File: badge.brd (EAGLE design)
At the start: 85 x 55 mm, 60 parts, among them J1 SJ-3523-SMT-TR, Q1 MMBT2222A-7-FSOT-23_DIO-M, Q2 MMBT2222A-7-FSOT-23_DIO-M, U1 MCP1703T-5002E, U2 SA602AD8-SOIC, U3 LM386M-1

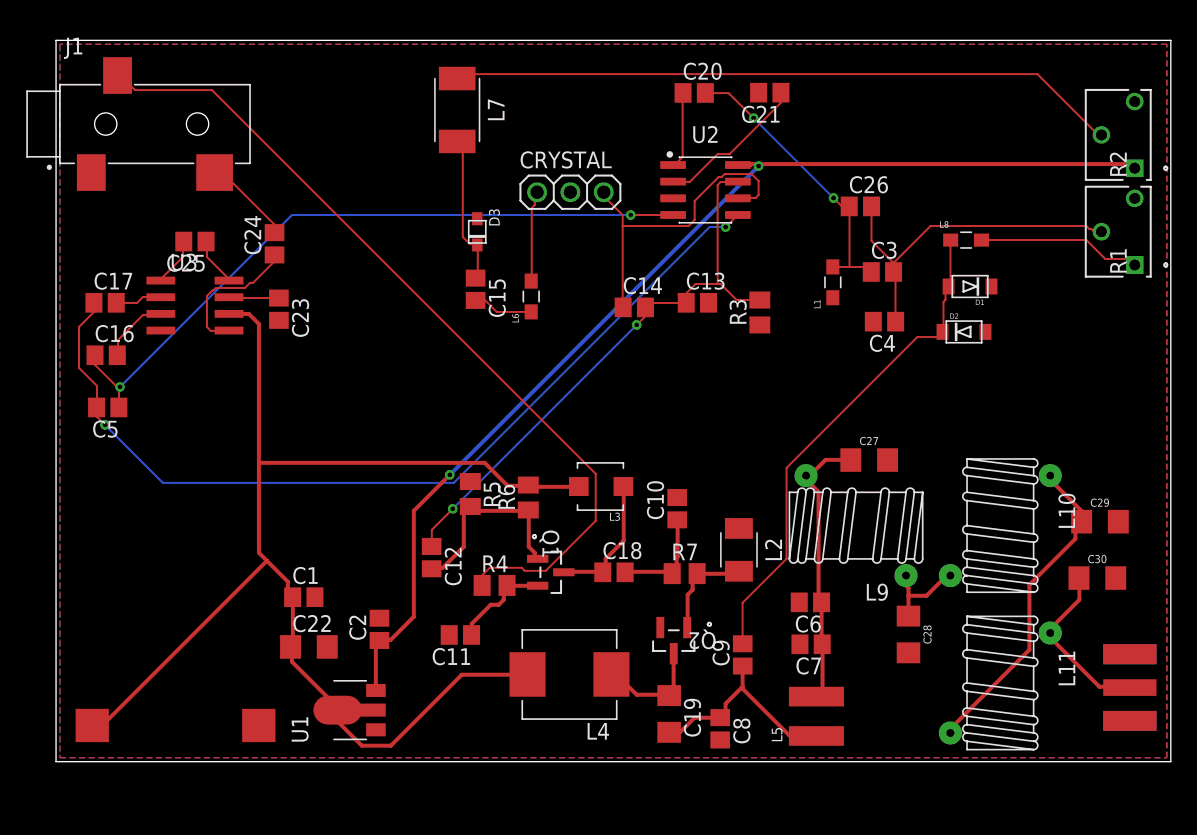
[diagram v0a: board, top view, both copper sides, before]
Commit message: updates
* added ATTiny keyer and buttons
* added breakout jumper
* added images
* added README
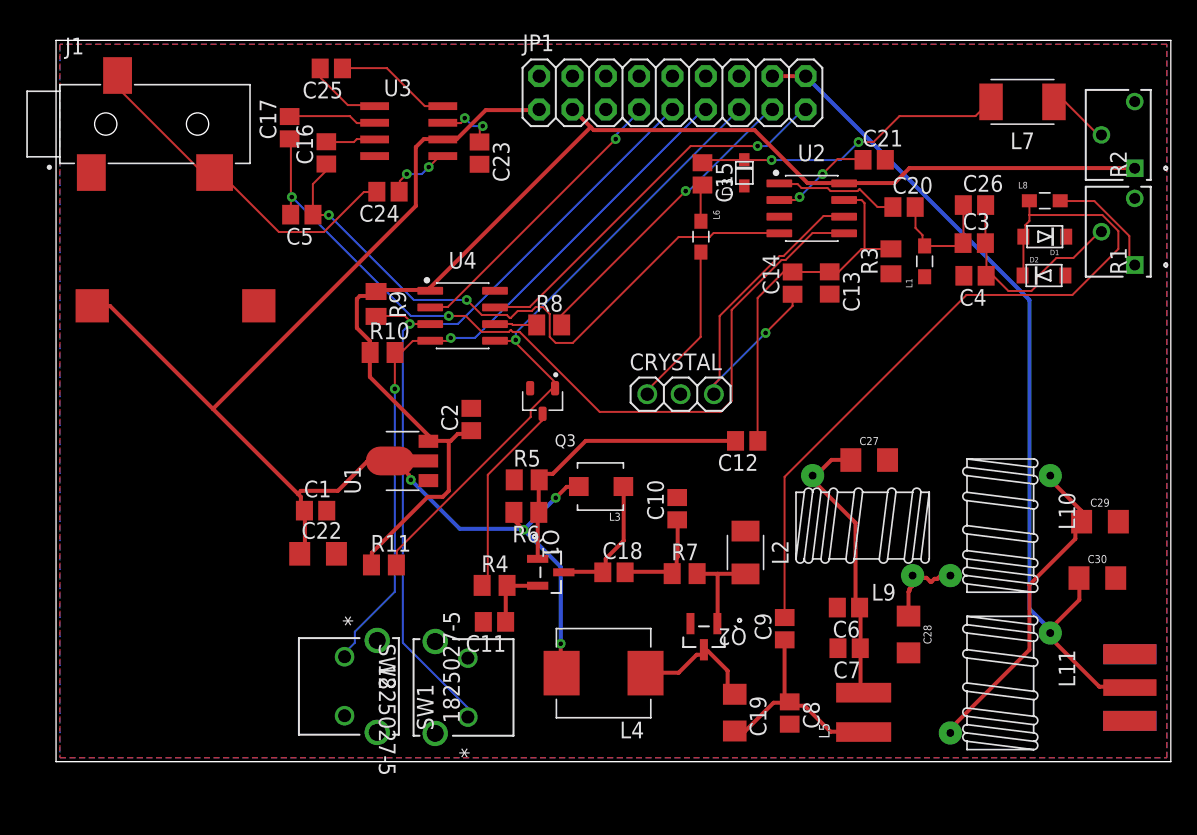
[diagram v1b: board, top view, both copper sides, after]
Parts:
- added JP1: (no value), adafruit:2X09-BIG
- added Q3: BSS138, Transistor:SOT23-3
- added R10, R11, R9: 10k, adafruit:M0805
- added R8: 4.7k, adafruit:M0805
- added SW1, SW2: 1825027-5, zort2:SW2_1825027-A_TEC
- added U4: ATTINY_402SOIC-8, zort2:SOIC127P599X175-8N
- moved L7 43.1 mm to (73.7, 50.3), turned to 180 degrees
- moved U$1 32.0 mm to (9.11, 34.8)
- moved C12 25.6 mm to (52.7, 24.5), turned to 180 degrees
- moved C16 22.8 mm to (20.6, 46.4), turned to 90 degrees
- moved U3 21.0 mm to (26.9, 48.1)
- moved C5 20.9 mm to (18.7, 41.7)
- moved D3 20.9 mm to (52.5, 44.9), turned to 90 degrees
- moved U1 19.4 mm to (26.4, 22.9)
- moved C15 19.4 mm to (49.3, 44.8)
- moved C17 19.4 mm to (17.8, 48.3), turned to 90 degrees
- moved C23 19.4 mm to (32.3, 46.4)
- moved C20 18.2 mm to (64.7, 42.3)
- moved CRYSTAL 17.5 mm to (47.6, 28.0)
- moved C2 17.5 mm to (31.7, 26.1)
- moved C25 16.8 mm to (21.0, 52.9)
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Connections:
- removed net 6V_DC: C2.1, R2.1, U1.3, U2.8
- removed net N$31: ANT.P, C30.1, L11.CA
- new net 5V_DC: C2.1, JP1.3, R10.1, R11.1, R2.1, R9.1, U1.3, U2.8, U4.1
- new net ANT: ANT.P, C30.1, JP1.16, JP1.18, L11.CA
- new net AT2: JP1.7, U4.2
- new net AT3: JP1.9, R9.2, SW1.1, U4.3
- new net AT4: JP1.11, R10.2, SW2.1, U4.4
- new net AT5: JP1.13, Q3.1, R11.2, U4.5
- new net AT6: R8.1, U4.6
- new net AT7: JP1.17, U4.7
- new net N$42: JP1.8
- new net N$43: JP1.10
- new net N$44: JP1.12
- new net N$45: JP1.14
- new net PROGRAM: JP1.15, R8.2
- net GND: now also JP1.2, JP1.4, JP1.5, JP1.6, Q3.2, SW1.2, SW1.3, SW1.4, SW2.2, SW2.3, SW2.4, U4.8
- net HEADPHONE: now also J1.3
- net KEY_IN: now also Q3.3; no longer J1.3
- net VIN: now also JP1.1
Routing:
- net 5V_DC: track 0.00 -> 98.5 mm
- net 6V_DC: track 83.1 -> 0.00 mm, vias 2 -> 0
- net ANT: track 0.00 -> 65.9 mm
- net AT3: track 0.00 -> 63.6 mm, vias 0 -> 1
- net AT4: track 0.00 -> 56.2 mm, vias 0 -> 2
- net AT5: track 0.00 -> 49.8 mm, vias 0 -> 1
- net KEY_IN: track 64.0 -> 15.0 mm
- net N$18: track 51.2 -> 4.69 mm
- net AT7: track 0.00 -> 30.0 mm, vias 0 -> 1
- net PROGRAM: track 0.00 -> 23.3 mm, vias 0 -> 1
- net AT2: track 0.00 -> 22.5 mm, vias 0 -> 1
- net ANT_IN: track 38.3 -> 58.0 mm
- net HEADPHONE: track 6.83 -> 26.5 mm
- net ANT_OUT: track 44.6 -> 27.8 mm, vias 2 -> 0
- net N$31: track 13.1 -> 0.00 mm
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
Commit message: moving to capacitive touch
Not ready for production

* replaced switches with capacitive touch buttons
* slight cleanup pass
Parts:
- removed SW1, SW2: 1825027-5, zort2:SW2_1825027-A_TEC
- added BTN1, BTN2: TOUCH_SMALL, zort2:TOUCH_SMALL
- added R12, R13, R14: 100, adafruit:M0805
- JP1: device adafruit:2X09-BIG -> adafruit:1X09-BIG
- R10, R9: value 10k -> 1M
- moved R11 18.0 mm to (37.5, 28.0)
- moved C22 17.7 mm to (8.15, 29.0), turned to 90 degrees
- moved C1 13.1 mm to (10.9, 28.8), turned to 90 degrees
- moved L8 8.41 mm to (79.2, 35.3)
- moved D1 8.28 mm to (79.3, 32.7)
- moved D2 8.10 mm to (79.2, 30.0)
- moved U1 6.73 mm to (19.8, 24.2)
- moved U$1 6.44 mm to (3.24, 32.1), turned to 180 degrees
- moved C2 5.98 mm to (25.7, 25.7), turned to 0 degrees
- moved Q3 5.10 mm to (32.5, 25.3)
- moved R9 1.55 mm to (24.0, 36.4), turned to 180 degrees
- moved JP1 1.00 mm to (47.0, 52.0)
- moved R10 0.91 mm to (24.0, 31.1)
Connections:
- net KEY_IN renamed Q1_GND
- removed net N$42: JP1.8
- removed net N$43: JP1.10
- removed net N$44: JP1.12
- removed net N$45: JP1.14
- new net KEY_SWITCH: JP1.3, Q3.1, R11.2, R14.2
- new net N$27: BTN1.P$1, R12.1, R9.2
- new net N$31: BTN2.P$1, R10.1, R13.2
- net 5V_DC: now also JP1.1; no longer JP1.3, R10.1, R11.1, R9.1
- net ANT: now also JP1.8, JP1.9; no longer JP1.16, JP1.18
- net AT2: now also R9.1; no longer JP1.7
- net AT3: now also R12.2; no longer JP1.9, R9.2, SW1.1
- net AT4: no longer JP1.11, SW2.1
- net AT5: now also R14.1; no longer JP1.13, Q3.1, R11.2
- net AT7: now also R13.1; no longer JP1.17
- net GND: now also BTN1.P$2, BTN2.P$2, JP1.7, R11.1; no longer JP1.2, SW1.2, SW1.3, SW1.4, SW2.2, SW2.3, SW2.4
- net PROGRAM: now also JP1.2; no longer JP1.15
- net VIN: no longer JP1.1
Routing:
- net AT3: track 63.6 -> 3.71 mm, vias 1 -> 0
- net AT4: track 56.2 -> 4.00 mm, vias 2 -> 0
- net N$31: track 0.00 -> 46.2 mm
- net AT5: track 49.8 -> 3.74 mm, vias 1 -> 0
- net N$27: track 0.00 -> 35.2 mm
- net KEY_SWITCH: track 0.00 -> 31.2 mm
- net AT7: track 30.0 -> 3.65 mm, vias 1 -> 0
- net VIN: track 103.5 -> 82.2 mm, vias 4 -> 6
- net AT2: track 22.5 -> 4.32 mm, vias 1 -> 0
- net ANT_IN: track 58.0 -> 41.4 mm
- net OUT_B: track 64.6 -> 49.2 mm
- net N$8: track 29.0 -> 18.5 mm, vias 1 -> 0
- net OUT_A: track 49.1 -> 40.5 mm
- net HEADPHONE: track 26.5 -> 33.5 mm
- net N$7: track 8.79 -> 3.38 mm
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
